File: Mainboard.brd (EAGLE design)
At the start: 162.6 x 57.2 mm, 77 parts, among them IC1 MS5611-01BA03, IC2 MCP73831, Q1 BSS84, U1 LM2937IMP-3.3, U2 USD-SOCKETNEW

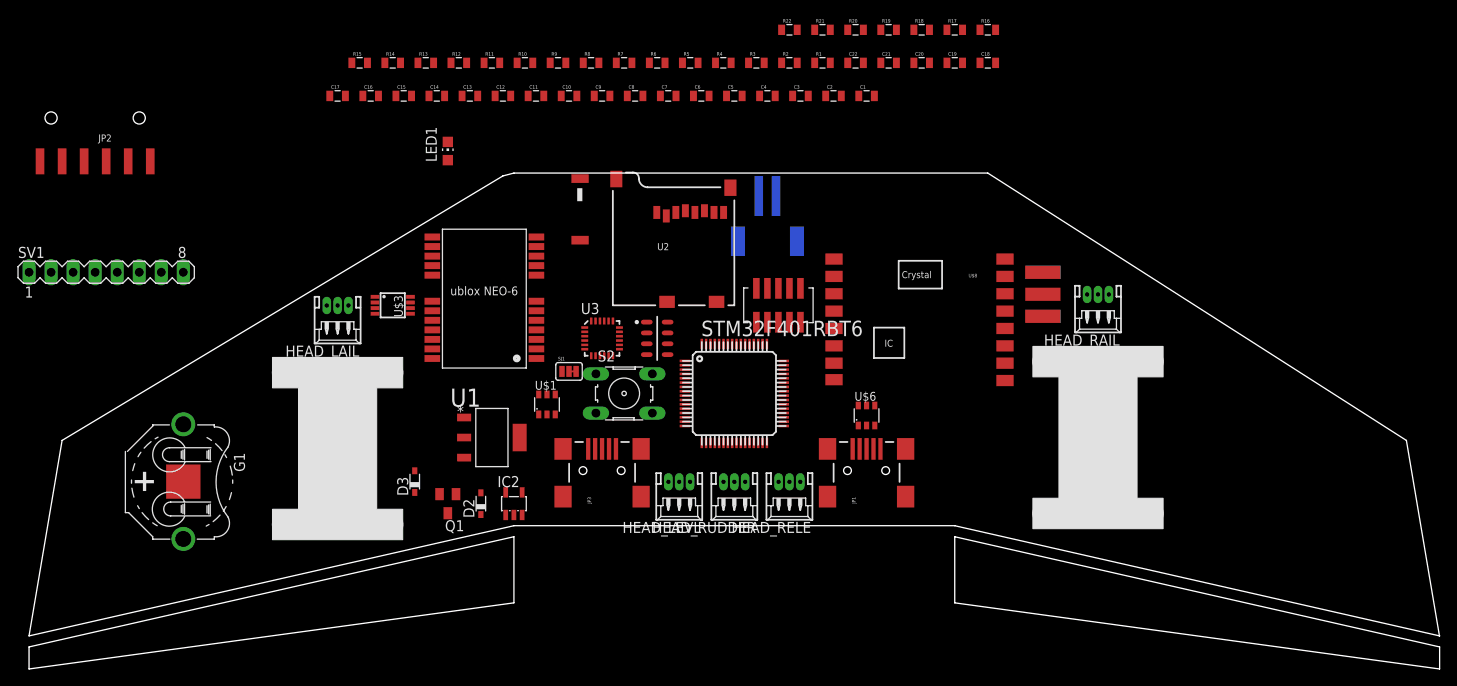
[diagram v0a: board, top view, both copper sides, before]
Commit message: Updated board and schematic, added power switch. changed connectors. Improved wing shape.
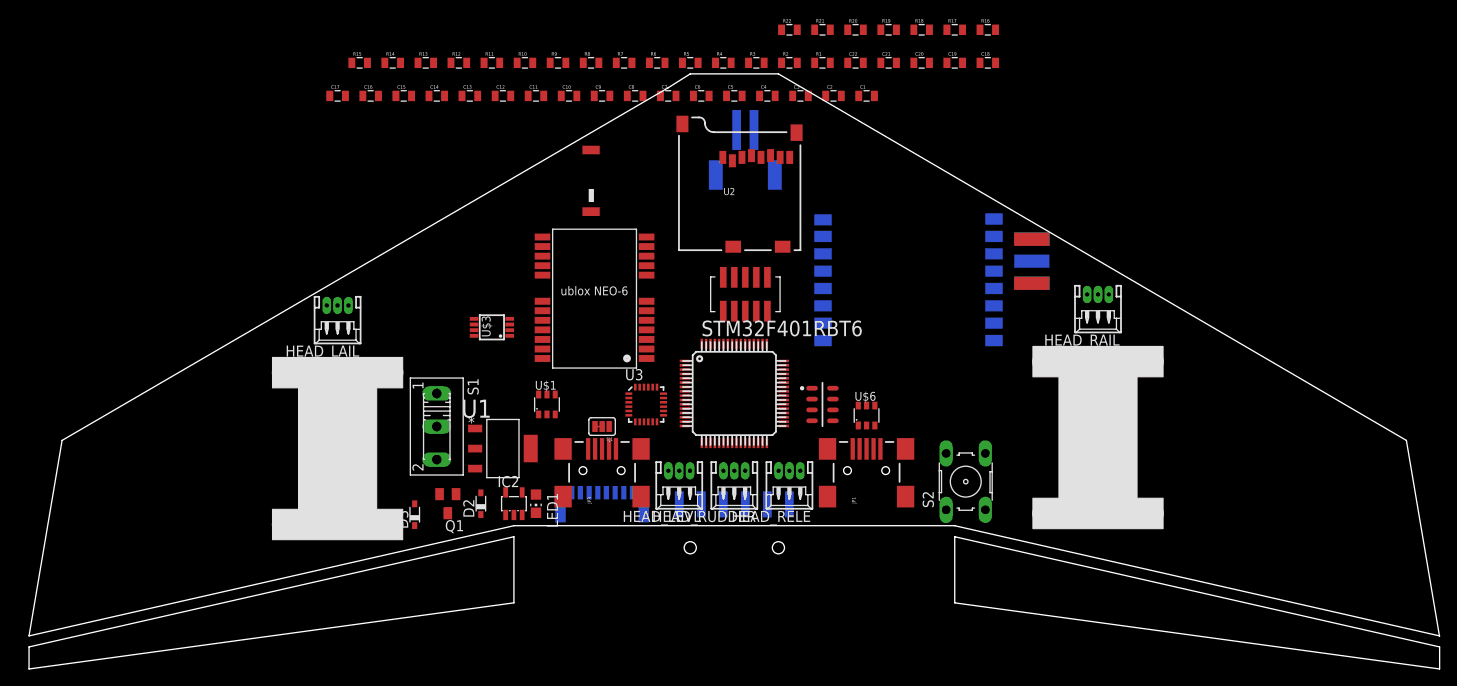
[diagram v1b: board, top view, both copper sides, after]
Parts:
- removed G1: BATTERY-HOLDER_11.6MM, battery:CELL_RETAINER_11.6MM
- removed SV1: (no value), con-lstb:MA08-1
- added JP4: (no value), SparkFun-Connectors:BM08B-SRSS-TB
- added S1: (no value), switch:255SB
- moved JP2 88.8 mm to (81.3, 10.2), flipped to the bottom, turned to 0 degrees
- moved LED1 41.9 mm to (58.4, 15.2), turned to 180 degrees
- moved S2 40.7 mm to (108.0, 17.8), turned to 90 degrees
- moved IC1 20.5 mm to (91.4, 26.7)
- moved U$5 12.7 mm to (64.8, 39.4)
- moved U$3 11.7 mm to (53.3, 35.6), turned to 90 degrees
- moved U2 9.92 mm to (88.9, 44.5)
- moved U3 9.16 mm to (71.1, 26.7)
- moved J1 8.03 mm to (82.5, 54.6)
- moved SJ1 7.41 mm to (66.0, 24.1), turned to 180 degrees
- moved U$8 4.02 mm to (101.6, 40.6), flipped to the bottom, turned to 180 degrees
- moved U$2 4.02 mm to (82.5, 39.4)
- moved D3 3.81 mm to (44.5, 14.0)
- moved U$4 2.84 mm to (64.8, 52.1), turned to 90 degrees
- moved J$1 1.80 mm to (115.6, 40.6), flipped to the bottom, turned to 90 degrees
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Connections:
- removed net N$29: G1.P+@1, G1.P+@2, U$5.22_V_BCKP
- new net N$2: C21.2, J1.2, S1.2
- net +4.1V: now also S1.3; no longer C21.2, J1.2
- net ADC1_IN10: now also JP4.6; no longer SV1.6
- net ADC1_IN11: now also JP4.5; no longer SV1.5
- net ADC1_IN12: now also JP4.4; no longer SV1.4
- net ADC1_IN13: now also JP4.3; no longer SV1.3
- net ADC1_IN14: now also JP4.2; no longer SV1.2
- net ADC1_IN15: now also JP4.1; no longer SV1.1
- net GND: now also JP4.7; no longer G1.N-, SV1.7
- net VDD: now also JP4.8; no longer SV1.8
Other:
- board size 162.6 x 57.2 mm -> 162.6 x 68.6 mm

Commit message: Updated PCB and added calculations spreadsheet
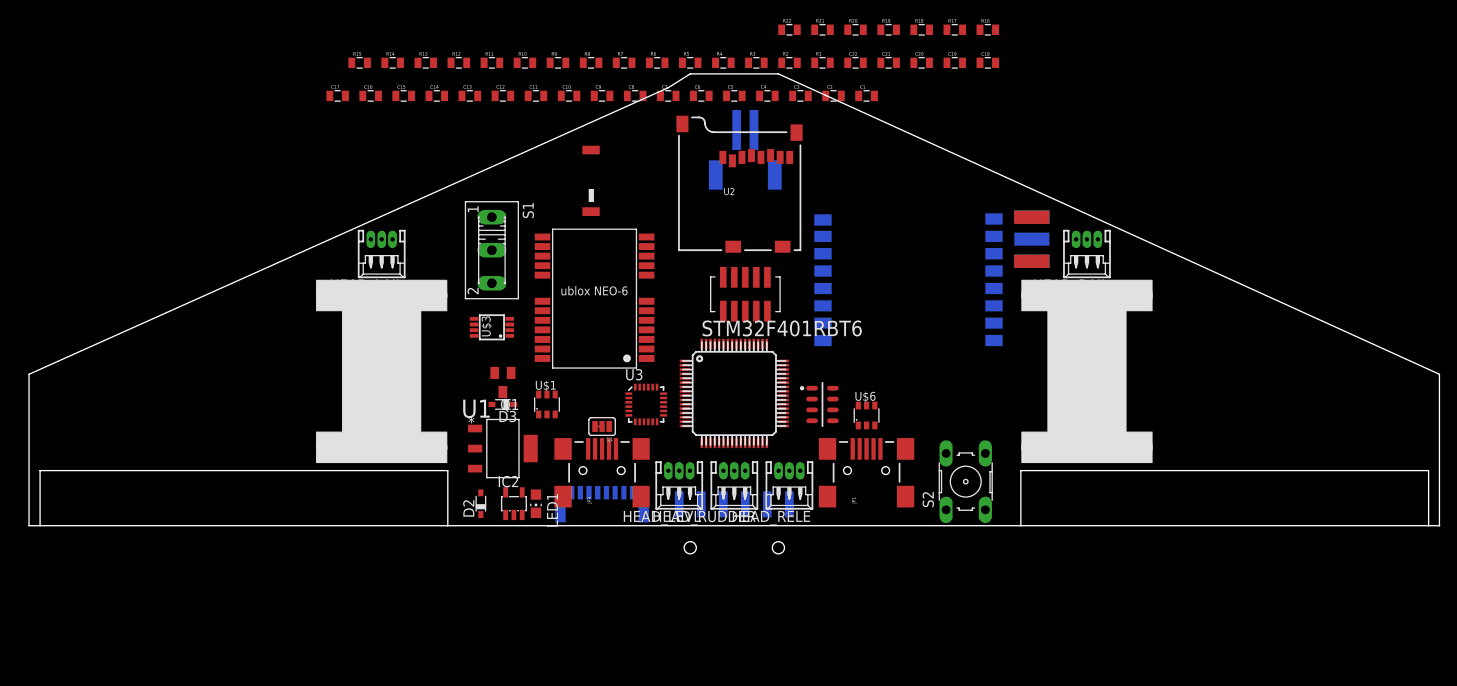
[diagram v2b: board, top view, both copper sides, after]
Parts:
- moved S1 21.3 mm to (53.3, 44.5)
- moved D3 16.3 mm to (54.6, 26.7), turned to 180 degrees
- moved Q1 15.3 mm to (54.6, 29.2)
- moved U$7 10.2 mm to (40.6, 30.5)
- moved HEAD_LAIL 9.16 mm to (40.6, 44.5)
- moved U$9 7.73 mm to (121.9, 30.5)
- moved HEAD_RAIL 6.48 mm to (121.9, 44.5)
- moved J$1 2.54 mm to (115.6, 43.2)
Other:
- board size 162.6 x 68.6 mm -> 162.6 x 52.1 mm

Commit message: Started initial routing
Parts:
- moved SJ1 1.61 mm to (67.6, 24.6), turned to 270 degrees
- moved U$6 0.26 mm to (96.5, 25.7), turned to 180 degrees
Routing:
- net VDD: track 0.00 -> 61.2 mm
- net GND: track 0.00 -> 11.9 mm
- net N$13: track 0.00 -> 8.86 mm
- net N$15: track 0.00 -> 5.37 mm
- net N$1: track 0.00 -> 4.53 mm
- net N$30: track 0.00 -> 1.10 mm
- net N$3: track 0.00 -> 0.57 mm
- added copper zone on layer 1, net GND
- added copper zone on layer 16, net GND
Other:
- outline, holes or cut-outs redrawn

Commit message: Board rearranged
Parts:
- moved U$4 55.7 mm to (10.3, 40.8)
- moved C14 53.0 mm to (90.0, 31.4)
- moved C21 51.3 mm to (74.1, 21.2)
- moved U$5 49.9 mm to (15.8, 29.5), turned to 90 degrees
- moved J$1 45.4 mm to (159.4, 31.3)
- moved C1 45.3 mm to (74.2, 22.8)
- moved U$8 43.7 mm to (143.5, 28.3)
- moved U$3 42.8 mm to (13.2, 20.7), turned to 270 degrees
- moved U2 41.8 mm to (50.4, 28.2), turned to 180 degrees
- moved R12 40.8 mm to (77.7, 36.6)
- moved R16 40.4 mm to (72.4, 56.3)
- moved R17 37.7 mm to (72.3, 54.3)
- moved C13 35.9 mm to (77.8, 38.6)
- moved R18 35.1 mm to (72.4, 52.4)
- moved R20 34.5 mm to (88.7, 36.0)
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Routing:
- net VDD: track 61.2 -> 0.00 mm
- net GND: track 11.9 -> 0.00 mm
- net N$13: track 8.86 -> 0.00 mm
- net N$15: track 5.37 -> 0.00 mm
- net N$1: track 4.53 -> 0.00 mm
- net N$30: track 1.10 -> 0.00 mm
- net N$3: track 0.57 -> 0.00 mm
- removed copper zone on layer 1, net GND
- removed copper zone on layer 16, net GND
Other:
- outline, holes or cut-outs redrawn

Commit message: Started wiring board
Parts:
- removed C1, C3: 0.1uF, SparkFun-Capacitors:0805
- removed C10, C5, C9: 1uF, SparkFun-Capacitors:0805
- removed C11, C21, C8: 10uF, SparkFun-Capacitors:0805
- removed C12, C13, C14, C16, C2, C6: 2.2nF, SparkFun-Capacitors:0805
- removed C15, C22: 100nF, SparkFun-Capacitors:0805
- removed C17, C18, C19, C20, C7: 100n, SparkFun-Capacitors:0805
- removed C4: 4.7uF, SparkFun-Capacitors:0805
- added C10_LM2937_3, C5_MCP73831_4, C9_LM2937_1: 1uF, SparkFun-Capacitors:0805
- added C11_LM2937_3, C21_MCP73831_VSS, C8_LM2937_1: 10uF, SparkFun-Capacitors:0805
- added C12_RFM69_8, C13_RFM69_8, C14_RFM69_1, C16_STM32_13, C2_MPU_20, C6_USB_VBUS: 2.2nF, SparkFun-Capacitors:0805
- added C15_MS5611_1, C22_JTAG_VCC: 100nF, SparkFun-Capacitors:0805
- added C17_STM32_32, C18_STM32_48, C19_STM32_64, C20_STM32_19, C7_RESET_DEBOUNCE: 100n, SparkFun-Capacitors:0805
- added C1_MPU_10, C3_MPU_3: 0.1uF, SparkFun-Capacitors:0805
- added C4_MCP73831_4: 4.7uF, SparkFun-Capacitors:0805
- moved R2 77.0 mm to (24.7, 21.7)
- moved R13 73.5 mm to (105.8, 23.7), turned to 180 degrees
- moved R10 60.5 mm to (10.3, 27.7)
- moved R11 58.8 mm to (10.3, 26.0)
- moved R7 52.3 mm to (101.3, 25.3)
- moved R8 52.1 mm to (97.6, 25.6)
- moved JP3 52.0 mm to (4.24, 30.7), flipped to the top, turned to 0 degrees
- moved R1 49.9 mm to (56.4, 30.5), turned to 270 degrees
- moved R15 47.8 mm to (24.7, 20.1)
- moved U$1 45.0 mm to (10.4, 30.8), flipped to the top
- moved R3 43.6 mm to (58.5, 30.5), turned to 270 degrees
- moved S1 39.9 mm to (93.1, 48.0)
- moved R17 29.9 mm to (54.2, 30.5), turned to 270 degrees
- moved R18 29.9 mm to (52.2, 30.5), turned to 270 degrees
- moved R19 28.4 mm to (87.5, 43.9), turned to 90 degrees
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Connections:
- net GND: now also C10_LM2937_3.2, C11_LM2937_3.2, C12_RFM69_8.2, C13_RFM69_8.2, C14_RFM69_1.2, C15_MS5611_1.1, C16_STM32_13.2, C17_STM32_32.1, C18_STM32_48.1, C19_STM32_64.1, C1_MPU_10.2, C20_STM32_19.1, C21_MCP73831_VSS.1, C22_JTAG_VCC.1, C2_MPU_20.2, C3_MPU_3.2, C4_MCP73831_4.2, C5_MCP73831_4.2, C6_USB_VBUS.1, C7_RESET_DEBOUNCE.2, C8_LM2937_1.2, C9_LM2937_1.2; no longer C1.2, C10.2, C11.2, C12.2, C13.2, C14.2, C15.1, C16.2, C17.1, C18.1, C19.1, C2.2, C20.1, C21.1, C22.1, C3.2, C4.2, C5.2, C6.1, C7.2, C8.2, C9.2
- net N$1: now also C4_MCP73831_4.1, C5_MCP73831_4.1; no longer C4.1, C5.1
- net N$13: now also C8_LM2937_1.1, C9_LM2937_1.1; no longer C8.1, C9.1
- net N$18: now also C1_MPU_10.1; no longer C1.1
- net N$2: now also C21_MCP73831_VSS.2; no longer C21.2
- net N$21: now also C2_MPU_20.1; no longer C2.1
- net N$28: now also C6_USB_VBUS.2; no longer C6.2
- net NRST: now also C7_RESET_DEBOUNCE.1; no longer C7.1
- net RFM_RST: now also C14_RFM69_1.1; no longer C14.1
- net VDD: now also C10_LM2937_3.1, C11_LM2937_3.1, C12_RFM69_8.1, C13_RFM69_8.1, C15_MS5611_1.2, C16_STM32_13.1, C17_STM32_32.2, C18_STM32_48.2, C19_STM32_64.2, C20_STM32_19.2, C22_JTAG_VCC.2, C3_MPU_3.1; no longer C10.1, C11.1, C12.1, C13.1, C15.2, C16.1, C17.2, C18.2, C19.2, C20.2, C22.2, C3.1
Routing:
- net GND: track 0.00 -> 139.4 mm
- net VDD: track 0.00 -> 60.6 mm
- net SDIO_CLK: track 0.00 -> 58.6 mm, vias 0 -> 2
- net SDIO_D1: track 0.00 -> 52.5 mm, vias 0 -> 2
- net SDIO_CMD: track 0.00 -> 51.2 mm, vias 0 -> 2
- net SDIO_D3: track 0.00 -> 47.4 mm, vias 0 -> 2
- net SDIO_D2: track 0.00 -> 46.4 mm, vias 0 -> 2
- net +4.1V: track 0.00 -> 45.9 mm
- net N$2: track 0.00 -> 33.6 mm
- net SCL: track 0.00 -> 25.0 mm, vias 0 -> 2
- net SDA: track 0.00 -> 24.6 mm, vias 0 -> 2
- net N$1: track 0.00 -> 23.4 mm
- net TIM4_CH3: track 0.00 -> 23.2 mm, vias 0 -> 1
- net JTDI: track 0.00 -> 22.8 mm
- net N$28: track 0.00 -> 19.9 mm
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
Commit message: Further routing
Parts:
- moved C6_USB_VBUS 81.7 mm to (12.8, 33.9), turned to 270 degrees
- moved JP2 33.7 mm to (103.4, 35.6), flipped to the top, turned to 90 degrees
- moved JP4 15.0 mm to (81.3, 16.3), flipped to the top
- moved R7 5.78 mm to (96.1, 22.8), turned to 270 degrees
- moved C22_JTAG_VCC 4.70 mm to (89.4, 40.8)
- moved U$6 4.04 mm to (97.2, 26.7)
- moved R8 2.74 mm to (97.5, 22.8), turned to 270 degrees
- moved U$2 1.37 mm to (82.9, 51.0)
- moved R19 0.26 mm to (87.8, 43.9), turned to 270 degrees
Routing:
- net VDD: track 60.6 -> 250.2 mm, vias 0 -> 2
- net GND: track 139.4 -> 258.1 mm, vias 0 -> 2
- net USART2_RX: track 0.00 -> 81.9 mm, vias 0 -> 2
- net USART2_TX: track 0.22 -> 78.6 mm, vias 0 -> 2
- net GPS_WAKE: track 0.00 -> 60.0 mm
- net TIMEPULSE: track 0.00 -> 58.4 mm
- net ADC1_IN12: track 0.00 -> 26.5 mm
- net ADC1_IN13: track 0.00 -> 24.9 mm
- net ADC1_IN10: track 0.00 -> 24.3 mm
- net ADC1_IN11: track 0.00 -> 23.9 mm
- net TIM3_CH4: track 18.6 -> 0.00 mm
- net N$13: track 7.99 -> 24.8 mm, vias 0 -> 2
- net ADC1_IN14: track 0.00 -> 15.1 mm
- net ADC1_IN15: track 0.00 -> 14.8 mm
- net JTMS: track 0.00 -> 14.1 mm
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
